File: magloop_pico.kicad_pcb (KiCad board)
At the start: 2 copper layers, 99.6 x 99.9 mm, 102 parts, among them J1 Conn_Coaxial_Power, J10 5V AUDIO MUTE, J2 Conn_02x03_Odd_Even, J3 POWER SW, J4 Conn_02x03_Odd_Even, J5 Conn_02x04_Odd_Even, J6 TO RF RELAY, J7 ETHERNET, J8 5-1634513-1, J9 12V AUDIO MUTE, Q1 NPN, Q10 PMOS, Q11 NPN, Q12 PMOS, Q2 NPN, Q3 NPN, Q4 NPN, Q5 NPN, Q6 NPN, Q7 NPN, Q8 PMOS, Q9 NPN, SW1 SW_DIP_x03, U1 AD9850MODULE, U2 A4988_Module, U3 LM7805, U4 PI_PICO, U5 LM4040DBZ-3, U7 LM358, U8 LM358

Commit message: Got all nets wired. Not clean yet.
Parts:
- removed R34, R39, R40: 10K, Resistor_SMD:R_1206_3216Metric_Pad1.30x1.75mm_HandSolder
- removed SW1: SW_DIP_x03, digikey-footprints:DIP-6_W7.62mm
- added D7: 1N4004, Diode_SMD:D_SMB, F.Cu at (122.2, 123.8)
- added D8: 1N4004, Diode_SMD:D_SMB, F.Cu at (122.2, 118.0)
- added R9: 0, Resistor_SMD:R_1206_3216Metric_Pad1.30x1.75mm_HandSolder, F.Cu at (95.2, 80.9)
- Q1, Q10, Q11, Q12, Q2, Q3, Q4, Q5, Q6, Q7, Q8, Q9, U5: footprint Package_TO_SOT_SMD:SOT-23_Handsoldering -> Package_TO_SOT_SMD:SOT-23
- U1: footprint magloop_pico:AD9850_MODULE -> AD9850:AD9850_MODULE
- U2: value A4988_Module -> TMC2209_Module; footprint magloop_pico:A4988_MODULE -> TMC2209:TMC2209_MODULE
- U4: footprint magloop_pico:PI_PICO -> PI_Pico:PI_PICO
- moved C20 17.8 mm to (123.3, 106.5), turned to 0 degrees
- moved Q12 12.3 mm to (121.7, 131.2)
- moved R38 11.2 mm to (127.1, 130.2), turned to 0 degrees
- moved R37 5.49 mm to (121.0, 135.5), turned to 0 degrees
- moved Q11 5.12 mm to (127.2, 134.5)
- moved J6 0.90 mm to (124.2, 111.2)
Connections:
- net +3V3 renamed +3.3V
- C20 pad 1: Net-(C20-Pad1) -> Net-(D7-K)
- J6 pad 2: Net-(C20-Pad1) -> Net-(D7-K)
- Q11 pad 3: Net-(Q11-Pad3) -> Net-(Q11-C)
- Q12 pad 1: Net-(Q12-Pad1) -> Net-(Q11-C)
- Q12 pad 3: Net-(C20-Pad1) -> Net-(D7-A)
- Q7 pad 3: Net-(Q7-Pad3) -> Net-(Q7-C)
- Q8 pad 1: Net-(Q8-Pad1) -> Net-(Q7-C)
- R33 pad 2: Net-(Q8-Pad1) -> Net-(Q7-C)
- R38 pad 2: Net-(Q12-Pad1) -> Net-(Q11-C)
- U2 pad 10: Net-(SW1-Pad3) -> unconnected-(U2-MS1-Pad10)
- U2 pad 11: Net-(SW1-Pad2) -> unconnected-(U2-MS2-Pad11)
- U2 pad 12: Net-(SW1-Pad1) -> unconnected-(U2-SPREAD-Pad12)
- U2 pad 13: Net-(R40-Pad2) -> /UART_TX
- U2 pad 14: /SLEEP -> unconnected-(U2-NC-Pad14)
- U2 pad 9: unconnected-(U2-Pad9) -> Net-(U2-EN!)
- U4 pad 11: /EXIT -> /UART_TX
- U4 pad 12: /SLEEP -> /EXIT
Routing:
- net /SLEEP: track 49.8 -> 0.00 mm
- net /EXIT: track 101.0 -> 148.2 mm
- net /UART_TX: track 0.00 -> 40.7 mm
- net Net-(SW1-Pad2): track 25.9 -> 0.00 mm
- net Net-(SW1-Pad3): track 25.0 -> 0.00 mm
- net Net-(SW1-Pad1): track 24.9 -> 0.00 mm
- net Net-(D7-K): track 0.00 -> 20.2 mm
- net /12V_FILT: track 123.9 -> 136.3 mm
- net Net-(Q11-C): track 0.00 -> 11.2 mm
- net Net-(C20-Pad1): track 10.8 -> 0.00 mm
- net Net-(Q7-C): track 0.00 -> 10.7 mm
- net Net-(D7-A): track 0.00 -> 8.85 mm
- net Net-(Q1-E): track 9.97 -> 16.9 mm, vias 0 -> 2
- net Net-(R40-Pad2): track 6.89 -> 0.00 mm
- net Net-(Q12-Pad1): track 6.88 -> 0.00 mm
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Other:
- board text added: "CONTROLLER 2.0"
- board text removed: "CONTROLLER 1.0"

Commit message: Layout clean
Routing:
- net /EXIT: track 148.2 -> 98.4 mm
- net /12V_FILT: track 136.3 -> 137.0 mm
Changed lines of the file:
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@@
     (property "ki_keywords" "cap capacitor")
     (attr smd)
-    (fp_text reference "C20" (at 0 3.302) (layer "F.SilkS")
-        (effects (font (size 1 1) (thickness 0.15)))
-    )
-    (fp_text value "0.1uF" (at 0 1.85) (layer "F.SilkS")
+    (fp_text reference "C20" (at 4.6875 0.375) (layer "F.SilkS")
+        (effects (font (size 1 1) (thickness 0.15)))
+    )
+    (fp_text value "0.1uF" (at 5.3875 -1.1) (layer "F.SilkS")
         (effects (font (size 1 1) (thickness 0.15)))
     )
@@
         (effects (font (size 1 1) (thickness 0.15)))
     )
-    (fp_text value "TO RF RELAY" (at -1.021 3.937 180) (layer "F.SilkS")
+    (fp_text value "TO RF RELAY" (at -3.725 -1.875 270) (layer "F.SilkS")
         (effects (font (size 1 1) (thickness 0.15)))
     )
@@
     (property "ki_keywords" "NPN Transistor")
     (attr smd)
-    (fp_text reference "Q11" (at 0 -2.4 180) (layer "F.SilkS")
+    (fp_text reference "Q11" (at -1.3375 -2.5 180) (layer "F.SilkS")
         (effects (font (size 1 1) (thickness 0.15)))
     )
@@
     (property "ki_keywords" "P-Channel MOSFET")
     (attr smd)
-    (fp_text reference "Q12" (at 0 -2.4 180) (layer "F.SilkS")
+    (fp_text reference "Q12" (at 2.7375 0.85 270) (layer "F.SilkS")
         (effects (font (size 1 1) (thickness 0.15)))
     )
@@
     (property "ki_keywords" "R res resistor")
     (attr smd)
-    (fp_text reference "R37" (at 3.429 -0.127 90) (layer "F.SilkS")
-        (effects (font (size 1 1) (thickness 0.15)))
-    )
-    (fp_text value "10K" (at 4.826 -0.127 90) (layer "F.SilkS")
+    (fp_text reference "R37" (at -1.35 -1.825 180) (layer "F.SilkS")
+        (effects (font (size 1 1) (thickness 0.15)))
+    )
+    (fp_text value "10K" (at 1.825 -1.8 180) (layer "F.SilkS")
         (effects (font (size 1 1) (thickness 0.15)))
     )
@@
     (property "ki_keywords" "R res resistor")
     (attr smd)
-    (fp_text reference "R38" (at 1.0585 -2.032) (layer "F.SilkS")
-        (effects (font (size 1 1) (thickness 0.15)))
-    )
-    (fp_text value "10K" (at -1.9895 -2.032) (layer "F.SilkS")
+    (fp_text reference "R38" (at 2.175 -1.925) (layer "F.SilkS")
+        (effects (font (size 1 1) (thickness 0.15)))
+    )
+    (fp_text value "10K" (at -1.15 -1.925) (layer "F.SilkS")
         (effects (font (size 1 1) (thickness 0.15)))
     )
@@
     (property "ki_keywords" "diode")
     (attr smd)
-    (fp_text reference "D7" (at 0 -3) (layer "F.SilkS")
+    (fp_text reference "D7" (at 4.9 0) (layer "F.SilkS")
         (effects (font (size 1 1) (thickness 0.15)))
     )
@@
     (property "ki_keywords" "R res resistor")
     (attr smd)
-    (fp_text reference "R9" (at 0 -1.82 90) (layer "F.SilkS")
+    (fp_text reference "R9" (at -2.35 -1.975 90) (layer "F.SilkS")
         (effects (font (size 1 1) (thickness 0.15)))
     )
@@
     (property "ki_keywords" "455-2247-ND XH")
     (attr through_hole)
-    (fp_text reference "J9" (at -3.58 -0.005 180) (layer "F.SilkS")
+    (fp_text reference "J9" (at -1.462 4.309 180) (layer "F.SilkS")
         (effects (font (size 1 1) (thickness 0.15)))
     )
@@
     (property "ki_keywords" "diode")
     (attr smd)
-    (fp_text reference "D8" (at 0 -3) (layer "F.SilkS")
+    (fp_text reference "D8" (at 2.35 -2.95) (layer "F.SilkS")
         (effects (font (size 1 1) (thickness 0.15)))
     )
@@
     (effects (font (size 1 1) (thickness 0.15)))
   )
-  (gr_text "DISPLAY" (at 124.206 137.414) (layer "F.SilkS")
+  (gr_text "DISPLAY" (at 122.05 137.55) (layer "F.SilkS")
     (effects (font (size 1 1) (thickness 0.15)))
   )
@@
   (via (at 185.801 71.755) (size 1) (drill 0.5) (layers "F.Cu" "B.Cu") (free) (net 1))
   (via (at 174.879 80.899) (size 1) (drill 0.5) (layers "F.Cu" "B.Cu") (free) (net 1))
-  (via (at 121.412 84.963) (size 1) (drill 0.5) (layers "F.Cu" "B.Cu") (free) (net 1))
+  (via (at 119.475 85) (size 1) (drill 0.5) (layers "F.Cu" "B.Cu") (free) (net 1))
   (via (at 142.748 145.288) (size 1) (drill 0.5) (layers "F.Cu" "B.Cu") (free) (net 1))
   (via (at 158.369 94.615) (size 1) (drill 0.5) (layers "F.Cu" "B.Cu") (free) (net 1))
@@
   (segment (start 129.225 110.706489) (end 158.712489 110.706489) (width 0.254) (layer "B.Cu") (net 25))
   (segment (start 127.718511 109.2) (end 129.225 110.706489) (width 0.254) (layer "B.Cu") (net 25))
-  (segment (start 113.518985 84.163489) (end 109.130511 84.163489) (width 0.254) (layer "F.Cu") (net 26))
-  (segment (start 105.791 109.347) (end 105.791 92.202) (width 0.254) (layer "F.Cu") (net 26))
-  (segment (start 114.210511 84.855015) (end 113.518985 84.163489) (width 0.254) (layer "F.Cu") (net 26))
-  (segment (start 105.791 92.202) (end 108.1405 89.8525) (width 0.254) (layer "F.Cu") (net 26))
-  (segment (start 109.130511 84.163489) (end 107.95 85.344) (width 0.254) (layer "F.Cu") (net 26))
-  (segment (start 114.210511 86.576489) (end 114.210511 84.855015) (width 0.254) (layer "F.Cu") (net 26))
-  (segment (start 108.1405 89.8525) (end 110.9345 89.8525) (width 0.254) (layer "F.Cu") (net 26))
-  (segment (start 96.52 118.618) (end 105.791 109.347) (width 0.254) (layer "F.Cu") (net 26))
-  (segment (start 110.9345 89.8525) (end 114.210511 86.576489) (width 0.254) (layer "F.Cu") (net 26))
   (segment (start 167.64 144.526) (end 165.354 146.812) (width 0.254) (layer "B.Cu") (net 26))
   (segment (start 96.139 140.589) (end 99.44196 140.589) (width 0.254) (layer "B.Cu") (net 26))
@@
   (via (at 121.2215 82.2325) (size 1) (drill 0.5) (layers "F.Cu" "B.Cu") (net 47))
   (via (at 128.143 95.631) (size 1) (drill 0.5) (layers "F.Cu" "B.Cu") (net 47))
-  (segment (start 123.571 84.582) (end 121.2215 82.2325) (width 1.016) (layer "B.Cu") (net 47))
-  (segment (start 128.143 84.582) (end 123.571 84.582) (width 1.016) (layer "B.Cu") (net 47))
+  (segment (start 121.2215 83.4215) (end 122.382 84.582) (width 1.016) (layer "B.Cu") (net 47))
+  (segment (start 122.382 84.582) (end 128.143 84.582) (width 1.016) (layer "B.Cu") (net 47))
+  (segment (start 121.2215 82.2325) (end 121.2215 83.4215) (width 1.016) (layer "B.Cu") (net 47))
   (segment (start 121.2215 82.2325) (end 120.015 81.026) (width 1.016) (layer "B.Cu") (net 47))
-  (segment (start 128.143 97.028) (end 128.143 84.582) (width 1.016) (layer "B.Cu") (net 47))
+  (segment (start 128.143 84.582) (end 128.143 97.028) (width 1.016) (layer "B.Cu") (net 47))
   (segment (start 175.504 119.878) (end 178.673 119.878) (width 0.508) (layer "F.Cu") (net 48))
   (segment (start 182.118 119.888) (end 178.715 119.888) (width 0.508) (layer "F.Cu") (net 48))
@@
       )
     )
-  )
-  (zone (net 0) (net_name "") (layer "F.Cu") (name "R40 Keepout") (hatch edge 0.508)
-    (connect_pads (clearance 0))
-    (min_thickness 0.254) (filled_areas_thickness no)
-    (keepout (tracks not_allowed) (vias not_allowed) (pads not_allowed) (copperpour not_allowed) (footprints allowed))
-    (fill (thermal_gap 0.508) (thermal_bridge_width 0.508))
-    (polygon
-      (pts
-        (xy 110.6932 80.6704)
-        (xy 109.5248 80.6704)
-        (xy 109.5248 78.8416)
-        (xy 110.6932 78.8416)
-      )
-    )

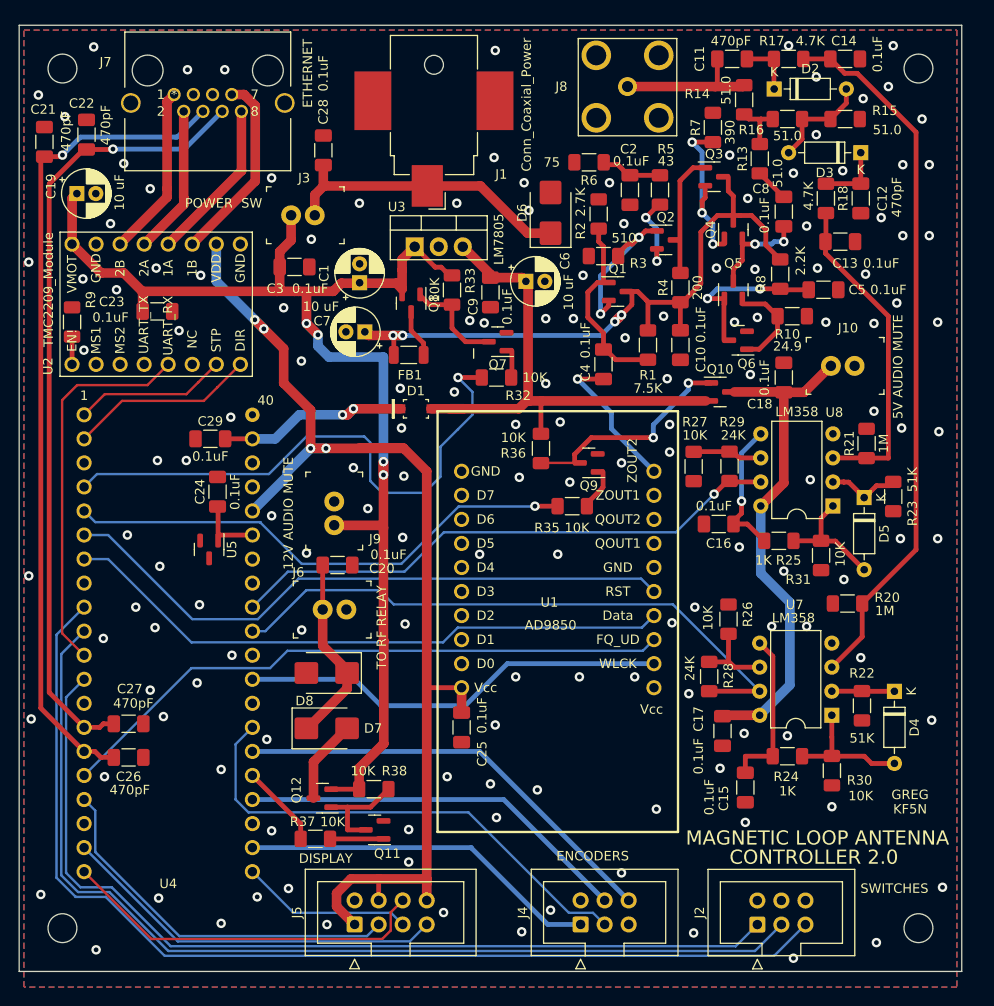
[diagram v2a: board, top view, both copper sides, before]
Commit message: This commit prior to experiment re-ordering schematic designators.
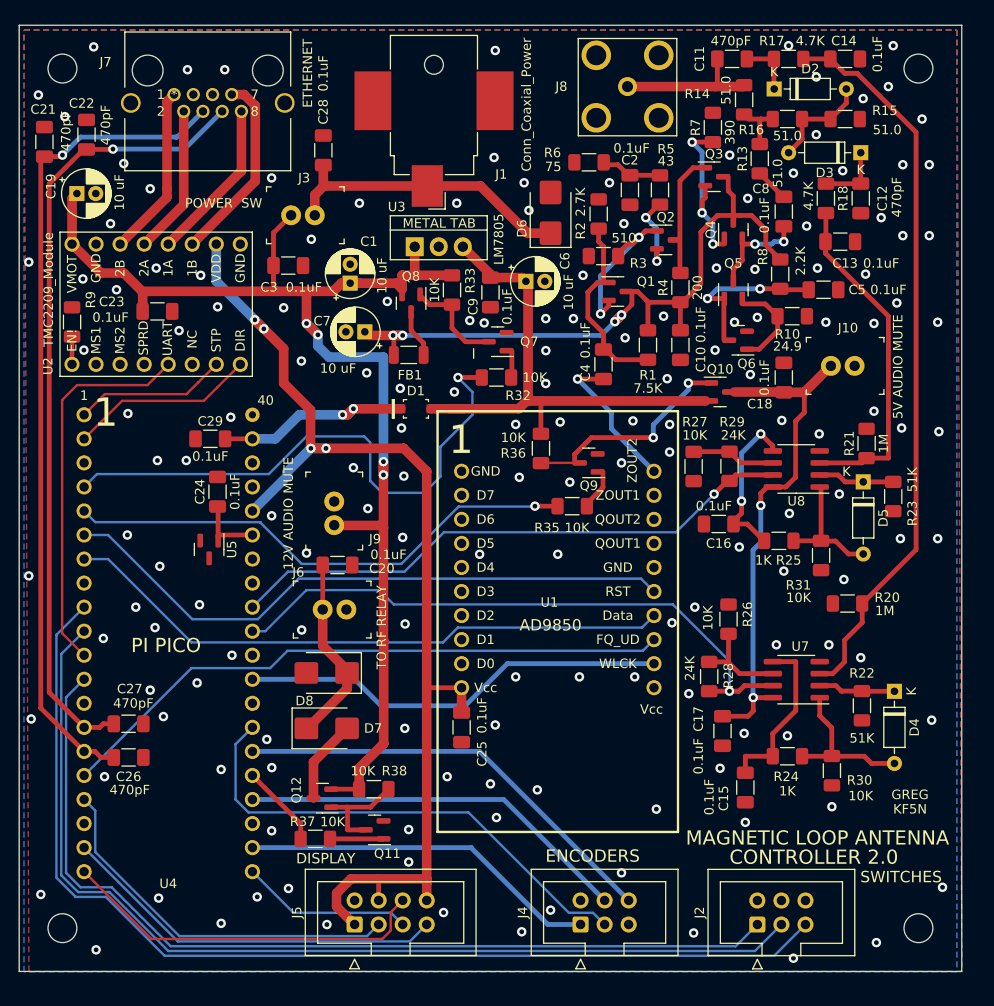
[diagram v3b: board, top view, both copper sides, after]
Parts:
- U7, U8: footprint Package_DIP:DIP-8_W7.62mm -> Package_SO:SOIC-8_3.9x4.9mm_P1.27mm
- moved U8 5.50 mm to (171.8, 96.4)
- moved U7 5.32 mm to (171.8, 118.7)
- moved D5 1.66 mm to (178.8, 97.8)
- moved C1 1.00 mm to (124.6, 76.8)
- moved C3 0.67 mm to (118.1, 74.9)
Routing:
- net +3.3V: track 124.0 -> 119.3 mm
- net Net-(D4-A): track 14.4 -> 16.8 mm
- net Net-(U8B-+): track 14.7 -> 17.0 mm, vias 1 -> 2
- net Net-(U7A-+): track 75.3 -> 77.3 mm
- net Net-(U7B--): track 8.51 -> 10.2 mm
- net Net-(U8A-+): track 34.5 -> 36.1 mm
- net Net-(D4-K): track 6.63 -> 8.15 mm
- net Net-(U8B--): track 7.39 -> 8.87 mm
- net /Forward: track 59.3 -> 60.5 mm
- net +5VA: track 53.0 -> 54.0 mm, vias 0 -> 2
- net Net-(U7B-+): track 17.2 -> 18.1 mm
- net Net-(D5-A): track 12.9 -> 13.7 mm
- net /Reverse: track 65.1 -> 65.5 mm, vias 0 -> 1
- net GND: vias 150 -> 162
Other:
- board text added: "PI PICO"

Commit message: Seems to be clean. Wait another 24 hours before release.
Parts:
- renumbered C28 to C1, C26 to C10, C27 to C11, C21 to C12, C22 to C13, C6 to C14, C7 to C15, C8 to C16, C9 to C17, C10 to C18, C11 to C19, C1 to C2, C12 to C20, C13 to C21, C29 to C22, C24 to C23, C14 to C24, C20 to C25, C15 to C26, C16 to C27, C17 to C28, C18 to C29, C19 to C3, C3 to C4, C4 to C5, C2 to C6, C25 to C7, C23 to C8, C5 to C9, D6 to D1, D1 to D2, D2 to D3, D3 to D4, D8 to D5, D7 to D6, D4 to D7, D5 to D8, J2 to J10, J7 to J2, J9 to J4, J8 to J5, J10 to J6, J6 to J7, J4 to J8, J5 to J9, Q7 to Q3, Q3 to Q4, Q8 to Q5, Q4 to Q6, Q5 to Q7, Q6 to Q8, R8 to R10, R9 to R11, R10 to R12, R14 to R13, R13 to R14, R35 to R15, R15 to R16, R16 to R17, R36 to R18, R18 to R19, R17 to R20, R37 to R21, R21 to R22, R38 to R23, R20 to R24, R23 to R25, R22 to R26, R30 to R27, R31 to R28, R25 to R29, R24 to R30, R26 to R31, R27 to R32, R28 to R33, R29 to R34, R32 to R4, R4 to R5, R5 to R6, R6 to R7, R33 to R8, R7 to R9, U8 to U6

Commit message: Released to PCBWay.
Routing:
- net GND: vias 162 -> 165
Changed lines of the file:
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@@
   (via (at 104.267 95.504) (size 1) (drill 0.5) (layers "F.Cu" "B.Cu") (free) (net 1))
   (via (at 157.734 80.264) (size 1) (drill 0.5) (layers "F.Cu" "B.Cu") (free) (net 1))
+  (via (at 124.15 51.59) (size 1) (drill 0.5) (layers "F.Cu" "B.Cu") (free) (net 1))
   (via (at 112.141 116.078) (size 1) (drill 0.5) (layers "F.Cu" "B.Cu") (free) (net 1))
   (via (at 104.394 141.732) (size 1) (drill 0.5) (layers "F.Cu" "B.Cu") (free) (net 1))
@@
   (via (at 107.442 54.229) (size 1) (drill 0.5) (layers "F.Cu" "B.Cu") (free) (net 1))
   (via (at 114.808 141.605) (size 1) (drill 0.5) (layers "F.Cu" "B.Cu") (free) (net 1))
+  (via (at 124.39 64.47) (size 1) (drill 0.5) (layers "F.Cu" "B.Cu") (free) (net 1))
   (via (at 169.65 114.975) (size 1) (drill 0.5) (layers "F.Cu" "B.Cu") (free) (net 1))
   (via (at 183.007 71.755) (size 1) (drill 0.5) (layers "F.Cu" "B.Cu") (free) (net 1))
@@
   (via (at 118.11 140.716) (size 1) (drill 0.5) (layers "F.Cu" "B.Cu") (free) (net 1))
   (via (at 120.523 72.136) (size 1) (drill 0.5) (layers "F.Cu" "B.Cu") (free) (net 1))
+  (via (at 134.74 83.72) (size 1) (drill 0.5) (layers "F.Cu" "B.Cu") (free) (net 1))
   (via (at 186.055 122.936) (size 1) (drill 0.5) (layers "F.Cu" "B.Cu") (free) (net 1))
   (via (at 187.198 140.589) (size 1) (drill 0.5) (layers "F.Cu" "B.Cu") (free) (net 1))

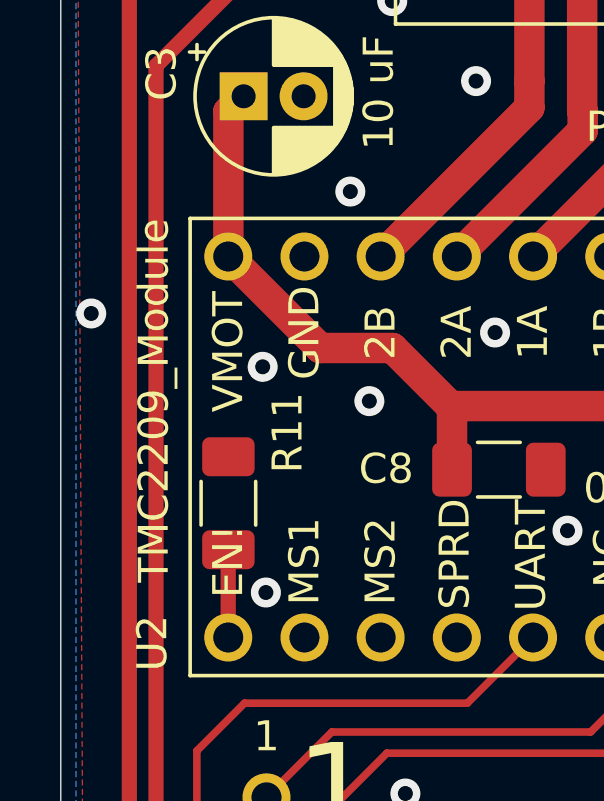
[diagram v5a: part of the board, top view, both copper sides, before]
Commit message: Fixed BOM problem with R5.
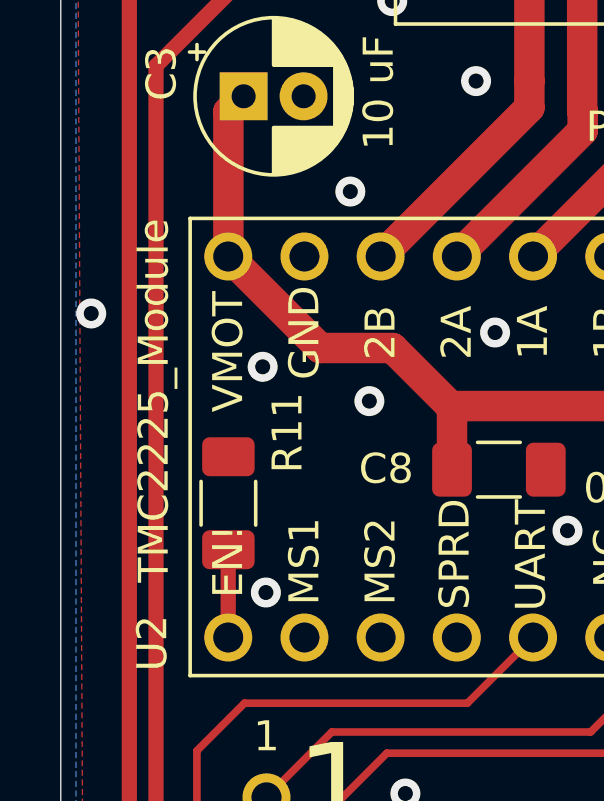
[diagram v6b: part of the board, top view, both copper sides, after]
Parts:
- U2: value TMC2209_Module -> TMC2225_Module
